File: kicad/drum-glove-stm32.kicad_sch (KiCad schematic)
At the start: 20 parts, among them J1 SPK, J2 PZ1, J3 PZ2, J4 PZ3, U1 STM32G431KBTx, U2 PAM8302AAY

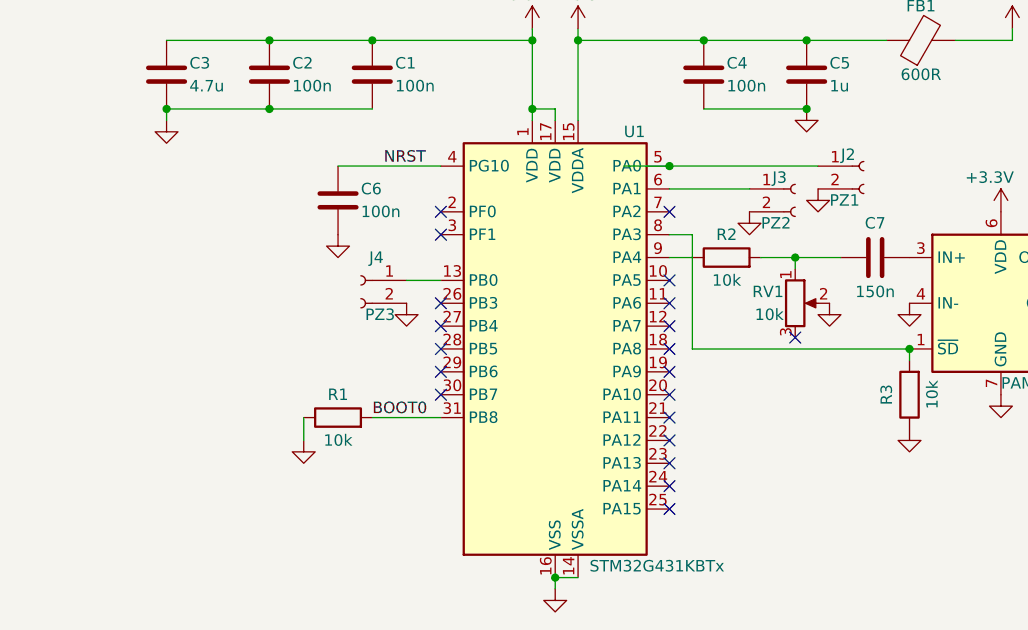
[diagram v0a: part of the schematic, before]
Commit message: refactor, refine tap detection
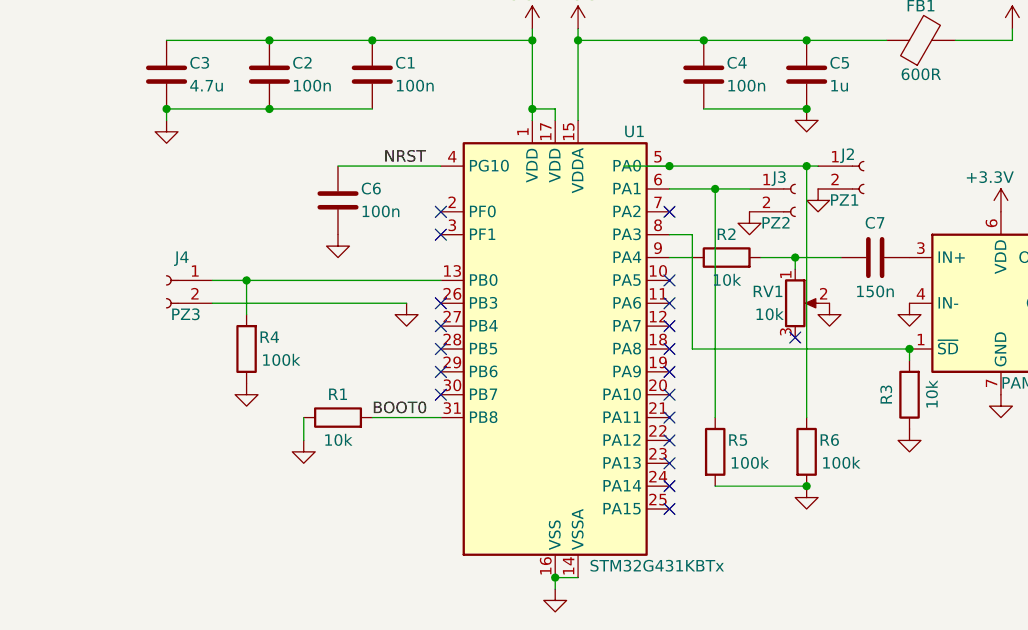
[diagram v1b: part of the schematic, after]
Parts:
- added R4, R5, R6: 100k, symbol Device:R
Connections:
- net GND: now also R4.1, R5.2, R6.2
- net at J2.1 (Pin_1), U1.5 (PA0): now also R6.1
- net at J4.1 (Pin_1), U1.13 (PB0): now also R4.2
- net at J3.1 (Pin_1), U1.6 (PA1): now also R5.1
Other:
- moved on the sheet: J4
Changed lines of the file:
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@@
 (kicad_sch (version 20230121) (generator eeschema)
   (paper "A4")
+  (junction (at 161.29 97.79) (diameter 0) (color 0 0 0 0)
+  )
   (junction (at 172.72 82.55) (diameter 0) (color 0 0 0 0)
   )
@@
   (junction (at 149.86 48.26) (diameter 0) (color 0 0 0 0)
   )
+  (junction (at 99.06 74.93) (diameter 0) (color 0 0 0 0)
+  )
   (junction (at 135.89 48.26) (diameter 0) (color 0 0 0 0)
   )
   (junction (at 205.74 86.36) (diameter 0) (color 0 0 0 0)
   )
+  (junction (at 151.13 64.77) (diameter 0) (color 0 0 0 0)
+  )
   (junction (at 113.03 48.26) (diameter 0) (color 0 0 0 0)
   )
@@
   )
   (junction (at 161.29 55.88) (diameter 0) (color 0 0 0 0)
+  )
+  (junction (at 161.29 62.23) (diameter 0) (color 0 0 0 0)
   )
   (junction (at 161.29 48.26) (diameter 0) (color 0 0 0 0)
@@
   (no_connect (at 146.05 74.93))
   (no_connect (at 160.02 81.28))
+  (wire (pts (xy 133.35 55.88) (xy 133.35 57.15))
+    (stroke (width 0) (type default))
+  )
+  (wire (pts (xy 146.05 64.77) (xy 151.13 64.77))
+    (stroke (width 0) (type default))
+  )
+  (wire (pts (xy 130.81 46.99) (xy 130.81 48.26))
+    (stroke (width 0) (type default))
+  )
+  (wire (pts (xy 205.74 77.47) (xy 205.74 78.74))
+    (stroke (width 0) (type default))
+  )
+  (wire (pts (xy 140.97 62.23) (xy 146.05 62.23))
+    (stroke (width 0) (type default))
+  )
+  (wire (pts (xy 148.59 82.55) (xy 172.72 82.55))
+    (stroke (width 0) (type default))
+  )
+  (wire (pts (xy 161.29 62.23) (xy 162.56 62.23))
+    (stroke (width 0) (type default))
+  )
+  (wire (pts (xy 101.6 48.26) (xy 90.17 48.26))
+    (stroke (width 0) (type default))
+  )
+  (wire (pts (xy 113.03 48.26) (xy 101.6 48.26))
+    (stroke (width 0) (type default))
+  )
+  (wire (pts (xy 135.89 46.99) (xy 135.89 48.26))
+    (stroke (width 0) (type default))
+  )
+  (wire (pts (xy 172.72 82.55) (xy 172.72 83.82))
+    (stroke (width 0) (type default))
+  )
   (wire (pts (xy 148.59 69.85) (xy 148.59 82.55))
     (stroke (width 0) (type default))
   )
-  (wire (pts (xy 133.35 55.88) (xy 133.35 57.15))
-    (stroke (width 0) (type default))
-  )
-  (wire (pts (xy 146.05 64.77) (xy 154.94 64.77))
-    (stroke (width 0) (type default))
-  )
-  (wire (pts (xy 130.81 46.99) (xy 130.81 48.26))
-    (stroke (width 0) (type default))
-  )
-  (wire (pts (xy 205.74 77.47) (xy 205.74 78.74))
-    (stroke (width 0) (type default))
-  )
-  (wire (pts (xy 140.97 62.23) (xy 146.05 62.23))
-    (stroke (width 0) (type default))
-  )
-  (wire (pts (xy 148.59 82.55) (xy 172.72 82.55))
-    (stroke (width 0) (type default))
-  )
-  (wire (pts (xy 101.6 48.26) (xy 90.17 48.26))
-    (stroke (width 0) (type default))
-  )
-  (wire (pts (xy 113.03 48.26) (xy 101.6 48.26))
-    (stroke (width 0) (type default))
-  )
-  (wire (pts (xy 135.89 46.99) (xy 135.89 48.26))
-    (stroke (width 0) (type default))
-  )
-  (wire (pts (xy 172.72 82.55) (xy 172.72 83.82))
+  (wire (pts (xy 161.29 62.23) (xy 161.29 90.17))
     (stroke (width 0) (type default))
   )
@@
     (stroke (width 0) (type default))
   )
+  (wire (pts (xy 151.13 64.77) (xy 151.13 90.17))
+    (stroke (width 0) (type default))
+  )
+  (wire (pts (xy 151.13 64.77) (xy 154.94 64.77))
+    (stroke (width 0) (type default))
+  )
+  (wire (pts (xy 99.06 74.93) (xy 120.65 74.93))
+    (stroke (width 0) (type default))
+  )
   (wire (pts (xy 130.81 55.88) (xy 133.35 55.88))
     (stroke (width 0) (type default))
@@
     (stroke (width 0) (type default))
   )
+  (wire (pts (xy 151.13 97.79) (xy 161.29 97.79))
+    (stroke (width 0) (type default))
+  )
   (wire (pts (xy 205.74 77.47) (xy 205.74 74.93))
     (stroke (width 0) (type default))
@@
     (stroke (width 0) (type default))
   )
+  (wire (pts (xy 99.06 74.93) (xy 99.06 78.74))
+    (stroke (width 0) (type default))
+  )
   (wire (pts (xy 90.17 57.15) (xy 90.17 55.88))
     (stroke (width 0) (type default))
@@
     (stroke (width 0) (type default))
   )
-  (wire (pts (xy 146.05 62.23) (xy 162.56 62.23))
+  (wire (pts (xy 146.05 62.23) (xy 161.29 62.23))
     (stroke (width 0) (type default))
   )
@@
     (stroke (width 0) (type default))
   )
-  (wire (pts (xy 116.84 74.93) (xy 120.65 74.93))
+  (wire (pts (xy 95.25 74.93) (xy 99.06 74.93))
     (stroke (width 0) (type default))
   )
@@
   )
   (wire (pts (xy 195.58 72.39) (xy 195.58 78.74))
+    (stroke (width 0) (type default))
+  )
+  (wire (pts (xy 95.25 77.47) (xy 116.84 77.47))
     (stroke (width 0) (type default))
   )
@@
     )
   )
+  (symbol (lib_id "Device:R") (at 161.29 93.98 0) (unit 1)
+    (in_bom yes) (on_board yes) (dnp no)
+    (property "Reference" "R6" (at 163.83 92.71 0)
+      (effects (font (size 1.27 1.27)))
+    )
+    (property "Value" "100k" (at 165.1 95.25 0)
+      (effects (font (size 1.27 1.27)))
+    )
+    (property "Footprint" "" (at 159.512 93.98 90)
+      (effects (font (size 1.27 1.27)) hide)
+    )
+    (property "Datasheet" "~" (at 161.29 93.98 0)
+      (effects (font (size 1.27 1.27)) hide)
+    )
+    (pin "1")
+    (pin "2")
+    (instances
+      (project "drum-glove-stm32"
+        (path "/222796f4-40c6-4317-acfb-860383721727"
+          (reference "R6") (unit 1)
+        )
+      )
+    )
+  )
   (symbol (lib_id "Device:C") (at 90.17 52.07 0) (unit 1)
     (in_bom yes) (on_board yes) (dnp no)
@@
     )
   )
+  (symbol (lib_id "Device:R") (at 151.13 93.98 0) (unit 1)
+    (in_bom yes) (on_board yes) (dnp no)
+    (property "Reference" "R5" (at 153.67 92.71 0)
+      (effects (font (size 1.27 1.27)))
+    )
+    (property "Value" "100k" (at 154.94 95.25 0)
+      (effects (font (size 1.27 1.27)))
+    )
+    (property "Footprint" "" (at 149.352 93.98 90)
+      (effects (font (size 1.27 1.27)) hide)
+    )
+    (property "Datasheet" "~" (at 151.13 93.98 0)
+      (effects (font (size 1.27 1.27)) hide)
+    )
+    (pin "1")
+    (pin "2")
+    (instances
+      (project "drum-glove-stm32"
+        (path "/222796f4-40c6-4317-acfb-860383721727"
+          (reference "R5") (unit 1)
+        )
+      )
+    )
+  )
   (symbol (lib_id "Device:R") (at 152.4 72.39 90) (unit 1)
     (in_bom yes) (on_board yes) (dnp no)
@@
     )
   )
-  (symbol (lib_id "Connector:Conn_01x02_Socket") (at 111.76 74.93 0) (mirror y) (unit 1)
-    (in_bom yes) (on_board yes) (dnp no)
-    (property "Reference" "J4" (at 114.3 72.39 0)
-      (effects (font (size 1.27 1.27)) (justify left))
-    )
-    (property "Value" "PZ3" (at 115.57 78.74 0)
-      (effects (font (size 1.27 1.27)) (justify left))
-    )
-    (property "Footprint" "" (at 111.76 74.93 0)
-      (effects (font (size 1.27 1.27)) hide)
-    )
-    (property "Datasheet" "~" (at 111.76 74.93 0)
+  (symbol (lib_id "Connector:Conn_01x02_Socket") (at 90.17 74.93 0) (mirror y) (unit 1)
+    (in_bom yes) (on_board yes) (dnp no)
+    (property "Reference" "J4" (at 92.71 72.39 0)
+      (effects (font (size 1.27 1.27)) (justify left))
+    )
+    (property "Value" "PZ3" (at 93.98 78.74 0)
+      (effects (font (size 1.27 1.27)) (justify left))
+    )
+    (property "Footprint" "" (at 90.17 74.93 0)
+      (effects (font (size 1.27 1.27)) hide)
+    )
+    (property "Datasheet" "~" (at 90.17 74.93 0)
       (effects (font (size 1.27 1.27)) hide)
     )
@@
         (path "/222796f4-40c6-4317-acfb-860383721727"
           (reference "#PWR016") (unit 1)
+        )
+      )
+    )
+  )
+  (symbol (lib_id "Device:R") (at 99.06 82.55 180) (unit 1)
+    (in_bom yes) (on_board yes) (dnp no)
+    (property "Reference" "R4" (at 101.6 81.28 0)
+      (effects (font (size 1.27 1.27)))
+    )
+    (property "Value" "100k" (at 102.87 83.82 0)
+      (effects (font (size 1.27 1.27)))
+    )
+    (property "Footprint" "" (at 100.838 82.55 90)
+      (effects (font (size 1.27 1.27)) hide)
+    )
+    (property "Datasheet" "~" (at 99.06 82.55 0)
+      (effects (font (size 1.27 1.27)) hide)
+    )
+    (pin "1")
+    (pin "2")
+    (instances
+      (project "drum-glove-stm32"
+        (path "/222796f4-40c6-4317-acfb-860383721727"
+          (reference "R4") (unit 1)
         )
       )
@@
         )
       )
+    )
+  )
+  (symbol (lib_id "power:GND") (at 161.29 97.79 0) (unit 1)
+    (in_bom yes) (on_board yes) (dnp no) (fields_autoplaced)
+    (property "Reference" "#PWR019" (at 161.29 104.14 0)
+      (effects (font (size 1.27 1.27)) hide)
+    )
+    (property "Value" "GND" (at 161.29 102.87 0)
+      (effects (font (size 1.27 1.27)) hide)
+    )
+    (property "Footprint" "" (at 161.29 97.79 0)
+      (effects (font (size 1.27 1.27)) hide)
+    )
+    (property "Datasheet" "" (at 161.29 97.79 0)
+      (effects (font (size 1.27 1.27)) hide)
+    )
+    (pin "1")
+    (instances
+      (project "drum-glove-stm32"
+        (path "/222796f4-40c6-4317-acfb-860383721727"
+          (reference "#PWR019") (unit 1)
+        )
+      )
+    )
+  )
+  (symbol (lib_id "power:GND") (at 99.06 86.36 0) (unit 1)
+    (in_bom yes) (on_board yes) (dnp no) (fields_autoplaced)
+    (property "Reference" "#PWR018" (at 99.06 92.71 0)
+      (effects (font (size 1.27 1.27)) hide)
+    )
+    (property "Value" "GND" (at 99.06 91.44 0)
+      (effects (font (size 1.27 1.27)) hide)
+    )
+    (property "Footprint" "" (at 99.06 86.36 0)
+      (effects (font (size 1.27 1.27)) hide)
+    )
+    (property "Datasheet" "" (at 99.06 86.36 0)
+      (effects (font (size 1.27 1.27)) hide)
+    )
+    (pin "1")
+    (instances
+      (project "drum-glove-stm32"
+        (path "/222796f4-40c6-4317-acfb-860383721727"
+          (reference "#PWR018") (unit 1)
+        )
+      )

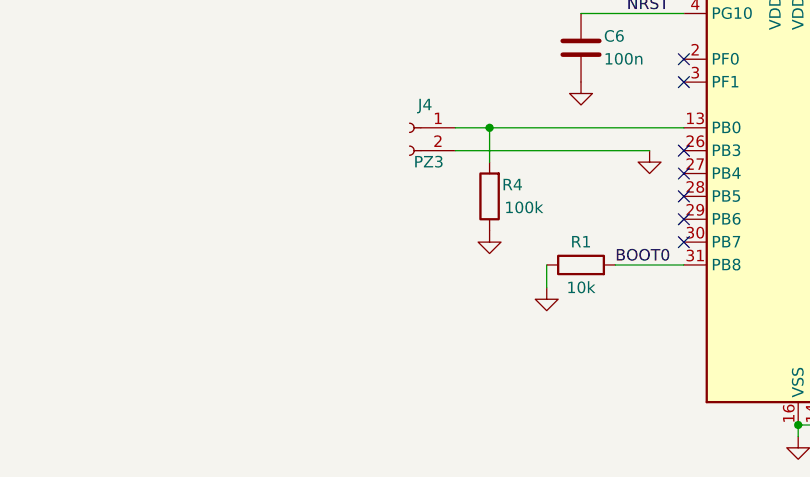
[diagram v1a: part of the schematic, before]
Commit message: update schematic
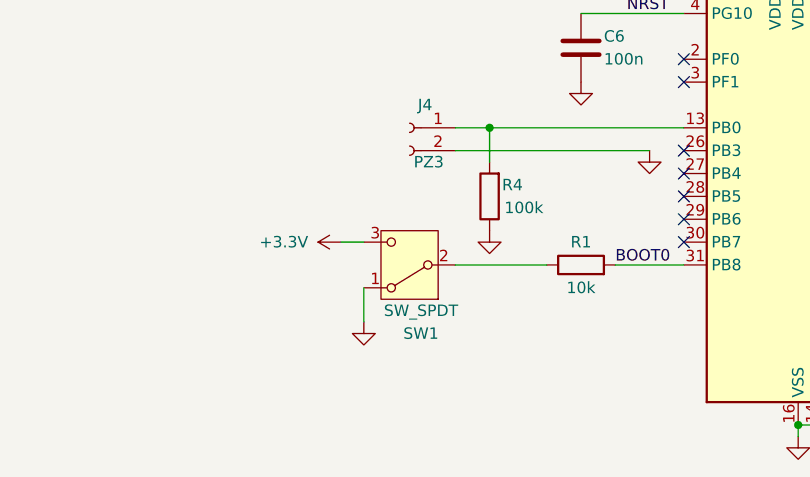
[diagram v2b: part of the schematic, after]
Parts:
- added SW1: SW_SPDT, symbol Switch:SW_SPDT
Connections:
- net +3.3V: now also SW1.3 (C)
- net GND: now also SW1.1 (A); no longer R1.1
- new net: R1.1, SW1.2 (B)
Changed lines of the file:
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@@
+    (stroke (width 0) (type default))
+  )
+  (wire (pts (xy 95.25 90.17) (xy 105.41 90.17))
     (stroke (width 0) (type default))
   )
@@
     (stroke (width 0) (type default))
   )
+  (wire (pts (xy 82.55 87.63) (xy 85.09 87.63))
+    (stroke (width 0) (type default))
+  )
   (wire (pts (xy 193.04 77.47) (xy 205.74 77.47))
     (stroke (width 0) (type default))
@@
     (stroke (width 0) (type default))
   )
-  (wire (pts (xy 105.41 90.17) (xy 105.41 92.71))
-    (stroke (width 0) (type default))
-  )
   (wire (pts (xy 184.15 48.26) (xy 177.8 48.26))
     (stroke (width 0) (type default))
@@
   )
   (wire (pts (xy 149.86 55.88) (xy 161.29 55.88))
+    (stroke (width 0) (type default))
+  )
+  (wire (pts (xy 85.09 92.71) (xy 85.09 96.52))
     (stroke (width 0) (type default))
   )
@@
     )
   )
+  (symbol (lib_id "Switch:SW_SPDT") (at 90.17 90.17 180) (unit 1)
+    (in_bom yes) (on_board yes) (dnp no)
+    (property "Reference" "SW1" (at 91.44 97.79 0)
+      (effects (font (size 1.27 1.27)))
+    )
+    (property "Value" "SW_SPDT" (at 91.44 95.25 0)
+      (effects (font (size 1.27 1.27)))
+    )
+    (property "Footprint" "" (at 90.17 90.17 0)
+      (effects (font (size 1.27 1.27)) hide)
+    )
+    (property "Datasheet" "~" (at 90.17 82.55 0)
+      (effects (font (size 1.27 1.27)) hide)
+    )
+    (pin "1")
+    (pin "2")
+    (pin "3")
+    (instances
+      (project "drum-glove-stm32"
+        (path "/222796f4-40c6-4317-acfb-860383721727"
+          (reference "SW1") (unit 1)
+        )
+      )
+    )
+  )
   (symbol (lib_id "Device:R") (at 152.4 72.39 90) (unit 1)
     (in_bom yes) (on_board yes) (dnp no)
@@
     )
   )
+  (symbol (lib_id "power:GND") (at 85.09 96.52 0) (unit 1)
+    (in_bom yes) (on_board yes) (dnp no) (fields_autoplaced)
+    (property "Reference" "#PWR07" (at 85.09 102.87 0)
+      (effects (font (size 1.27 1.27)) hide)
+    )
+    (property "Value" "GND" (at 85.09 101.6 0)
+      (effects (font (size 1.27 1.27)) hide)
+    )
+    (property "Footprint" "" (at 85.09 96.52 0)
+      (effects (font (size 1.27 1.27)) hide)
+    )
+    (property "Datasheet" "" (at 85.09 96.52 0)
+      (effects (font (size 1.27 1.27)) hide)
+    )
+    (pin "1")
+    (instances
+      (project "drum-glove-stm32"
+        (path "/222796f4-40c6-4317-acfb-860383721727"
+          (reference "#PWR07") (unit 1)
+        )
+      )
+    )
+  )
   (symbol (lib_id "Connector:Conn_01x02_Socket") (at 167.64 62.23 0) (unit 1)
     (in_bom yes) (on_board yes) (dnp no)
@@
         (path "/222796f4-40c6-4317-acfb-860383721727"
           (reference "#PWR015") (unit 1)
+        )
+      )
+    )
+  )
+  (symbol (lib_id "power:+3.3V") (at 82.55 87.63 90) (unit 1)
+    (in_bom yes) (on_board yes) (dnp no)
+    (property "Reference" "#PWR020" (at 86.36 87.63 0)
+      (effects (font (size 1.27 1.27)) hide)
+    )
+    (property "Value" "+3.3V" (at 76.2 87.63 90)
+      (effects (font (size 1.27 1.27)))
+    )
+    (property "Footprint" "" (at 82.55 87.63 0)
+      (effects (font (size 1.27 1.27)) hide)
+    )
+    (property "Datasheet" "" (at 82.55 87.63 0)
+      (effects (font (size 1.27 1.27)) hide)
+    )
+    (pin "1")
+    (instances
+      (project "drum-glove-stm32"
+        (path "/222796f4-40c6-4317-acfb-860383721727"
+          (reference "#PWR020") (unit 1)
         )
       )
@@
         )
       )
-    )
-  )
-  (symbol (lib_id "power:GND") (at 105.41 92.71 0) (unit 1)
-    (in_bom yes) (on_board yes) (dnp no) (fields_autoplaced)
-    (property "Reference" "#PWR07" (at 105.41 99.06 0)
-      (effects (font (size 1.27 1.27)) hide)
-    )
-    (property "Value" "GND" (at 105.41 97.79 0)
-      (effects (font (size 1.27 1.27)) hide)
-    )
-    (property "Footprint" "" (at 105.41 92.71 0)
-      (effects (font (size 1.27 1.27)) hide)
-    )
-    (property "Datasheet" "" (at 105.41 92.71 0)
-      (effects (font (size 1.27 1.27)) hide)
-    )
-    (pin "1")
-    (instances
-      (project "drum-glove-stm32"
-        (path "/222796f4-40c6-4317-acfb-860383721727"
-          (reference "#PWR07") (unit 1)
-        )
-      )
